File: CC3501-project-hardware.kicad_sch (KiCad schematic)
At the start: 0 parts

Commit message: Add USB C and make connections to ground.
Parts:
- added J1: USB_C_Receptacle_USB2.0_16P, Connector_USB:USB_C_Receptacle_G-Switch_GT-USB-7010ASV, symbol Connector:USB_C_Receptacle_USB2.0_16P
- added R1, R2: 5K1, Resistor_SMD:R_01005_0402Metric, symbol Device:R
- added U1: RP2040, Package_DFN_QFN:QFN-56-1EP_7x7mm_P0.4mm_EP3.2x3.2mm, symbol MCU_RaspberryPi:RP2040
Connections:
- new net: U1.1 (IOVDD), U1.10 (IOVDD), U1.22 (IOVDD), U1.33 (IOVDD), U1.42 (IOVDD), U1.49 (IOVDD)
- new net: U1.23 (DVDD), U1.50 (DVDD)
- new net: J1.A5 (CC1), R2.1
- new net: J1.B5 (CC2), R1.1
- new net: J1.A4 (VBUS), J1.A9 (VBUS), J1.B4 (VBUS), J1.B9 (VBUS)
- new net GND: J1.A1 (GND), J1.A12 (GND), J1.B1 (GND), J1.B12 (GND), J1.SH (SHIELD), R1.2, R2.2
- new net USB_D_N: J1.A7 (D-), J1.B7 (D-)
- new net USB_D_P: J1.A6 (D+), J1.B6 (D+)
- no-connect marks 0 -> 2

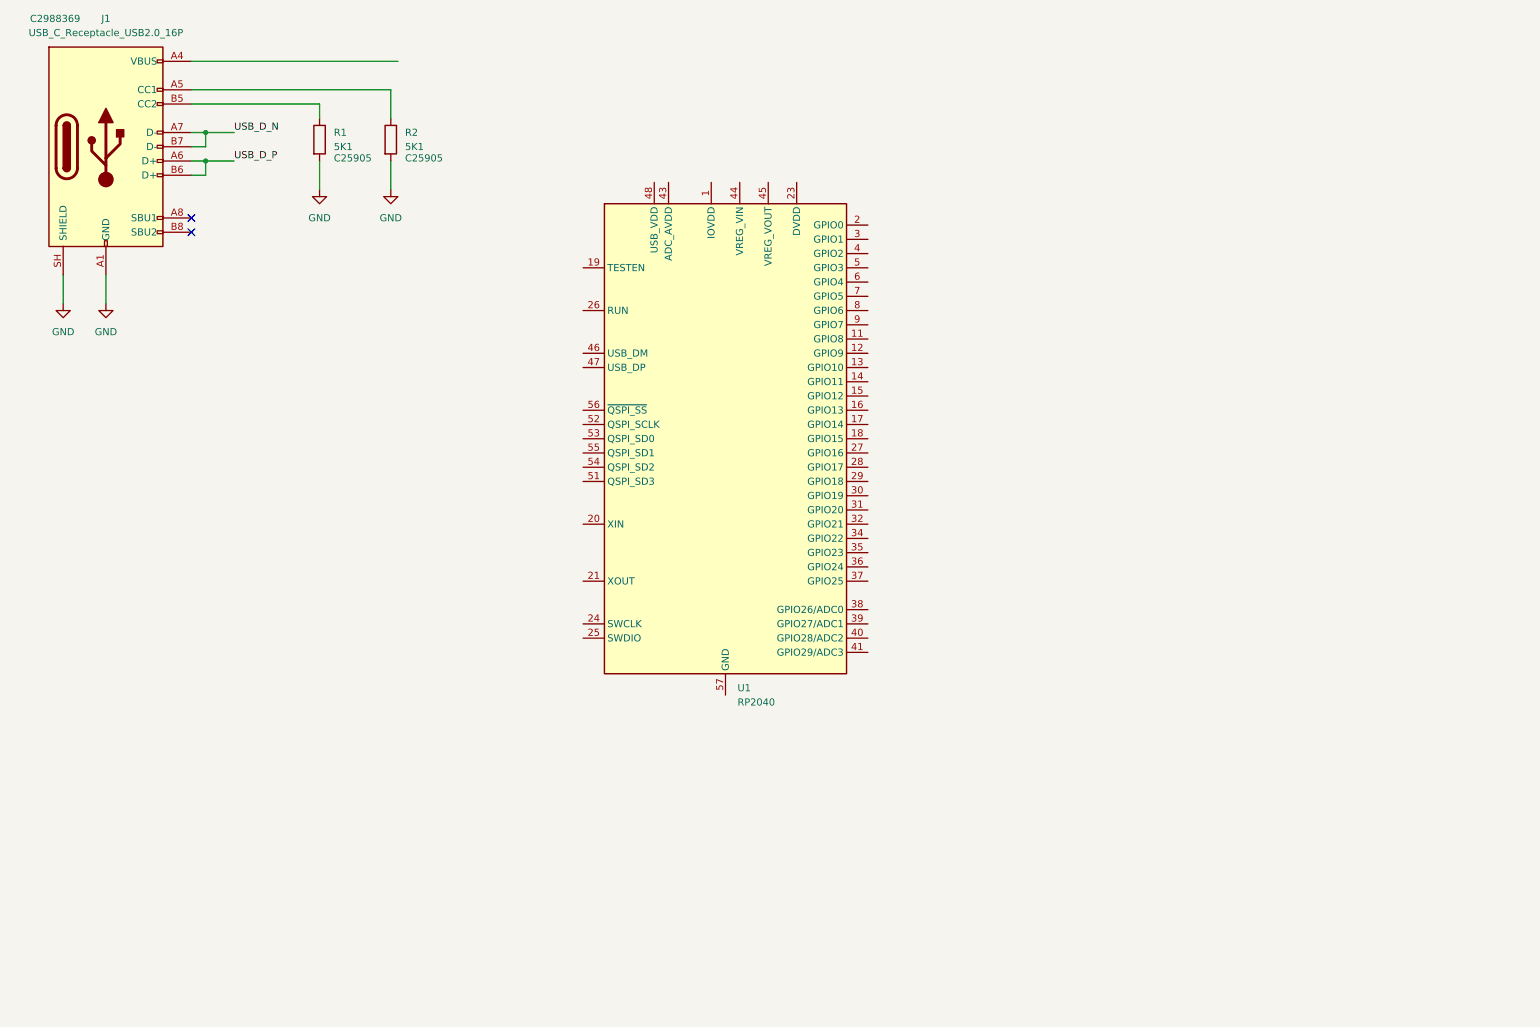
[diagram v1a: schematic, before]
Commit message: Add voltage regulator to USB input.
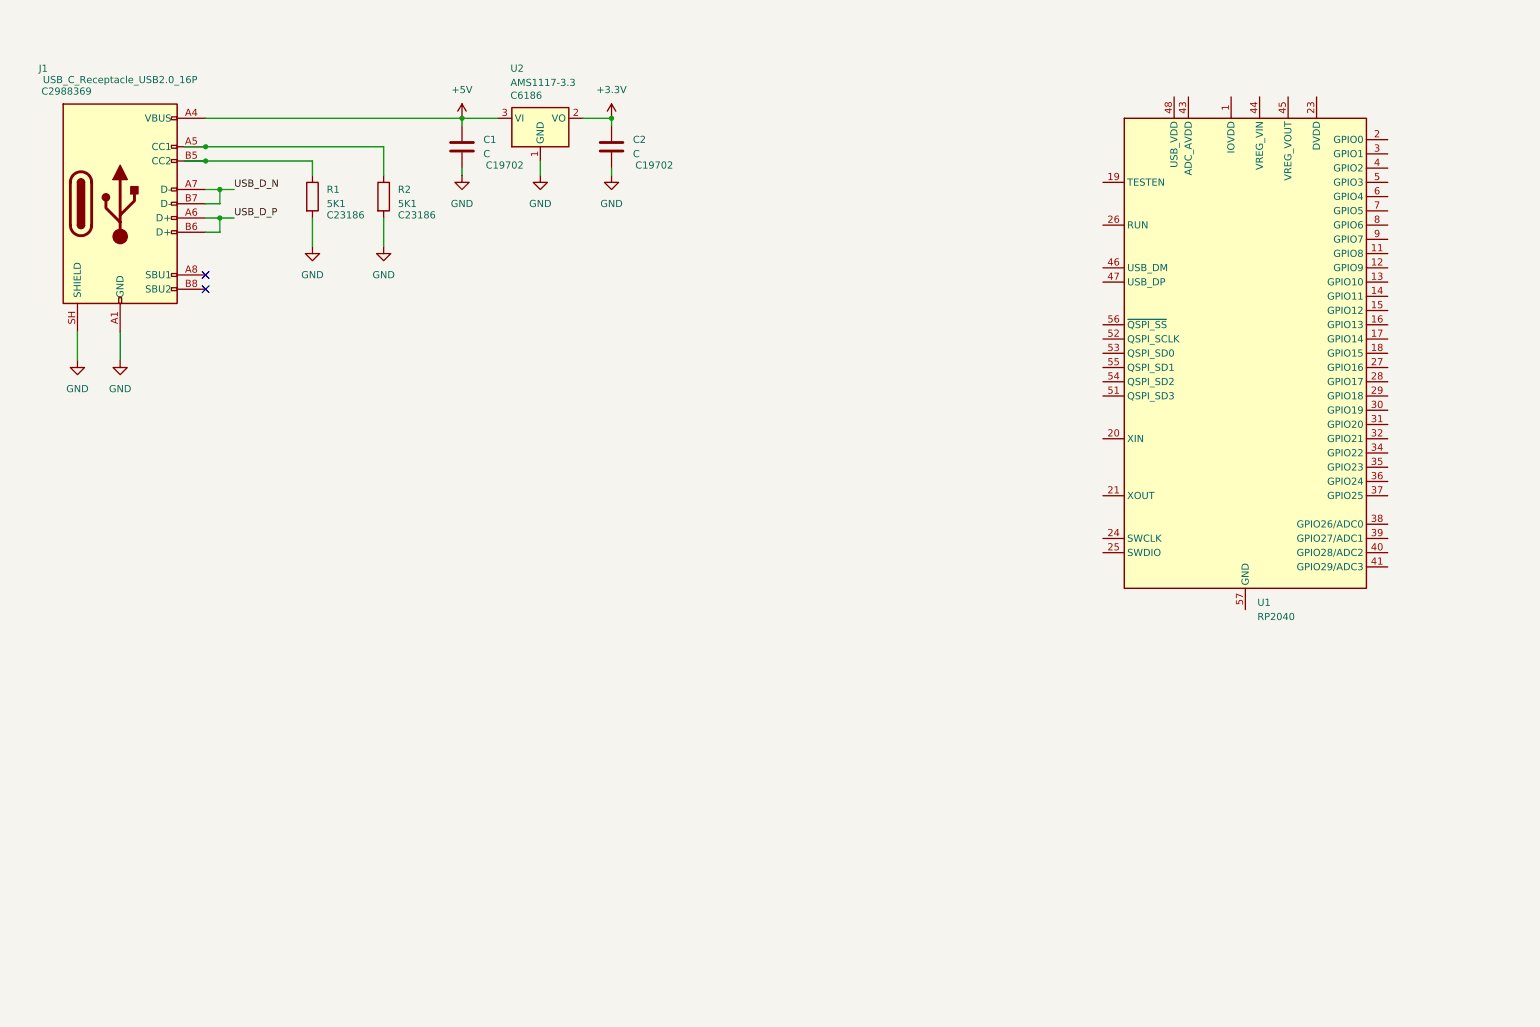
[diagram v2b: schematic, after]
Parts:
- added C1, C2: C, Capacitor_SMD:C_0201_0603Metric, symbol Device:C
- added U2: AMS1117-3.3, Package_TO_SOT_SMD:SOT-223-3_TabPin2, symbol Regulator_Linear:AMS1117-3.3
- R1, R2: footprint Resistor_SMD:R_01005_0402Metric -> Resistor_SMD:R_0201_0603Metric; LSCS PN C25905 -> C23186
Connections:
- net GND: now also C1.2, C2.2, U2.1 (GND)
- net +5V: now reaches J1.A4 (VBUS), J1.A9 (VBUS), J1.B4 (VBUS), J1.B9 (VBUS)
- net +5V: now also C1.1, U2.3 (VI)
- new net +3.3V: C2.1, U2.2 (VO)
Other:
- moved on the sheet: J1, R1, U1

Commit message: Add connection from USB DN/DP pins to RP2040 and include series 27R resisotor.
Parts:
- added R3, R4: 27R, Resistor_SMD:R_0201_0603Metric, symbol Device:R
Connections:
- net USB_D_N: now also R3.2
- net USB_D_P: now also R4.2
- net at U1.46 (USB_DM): now also R3.1
- net at U1.47 (USB_DP): now also R4.1

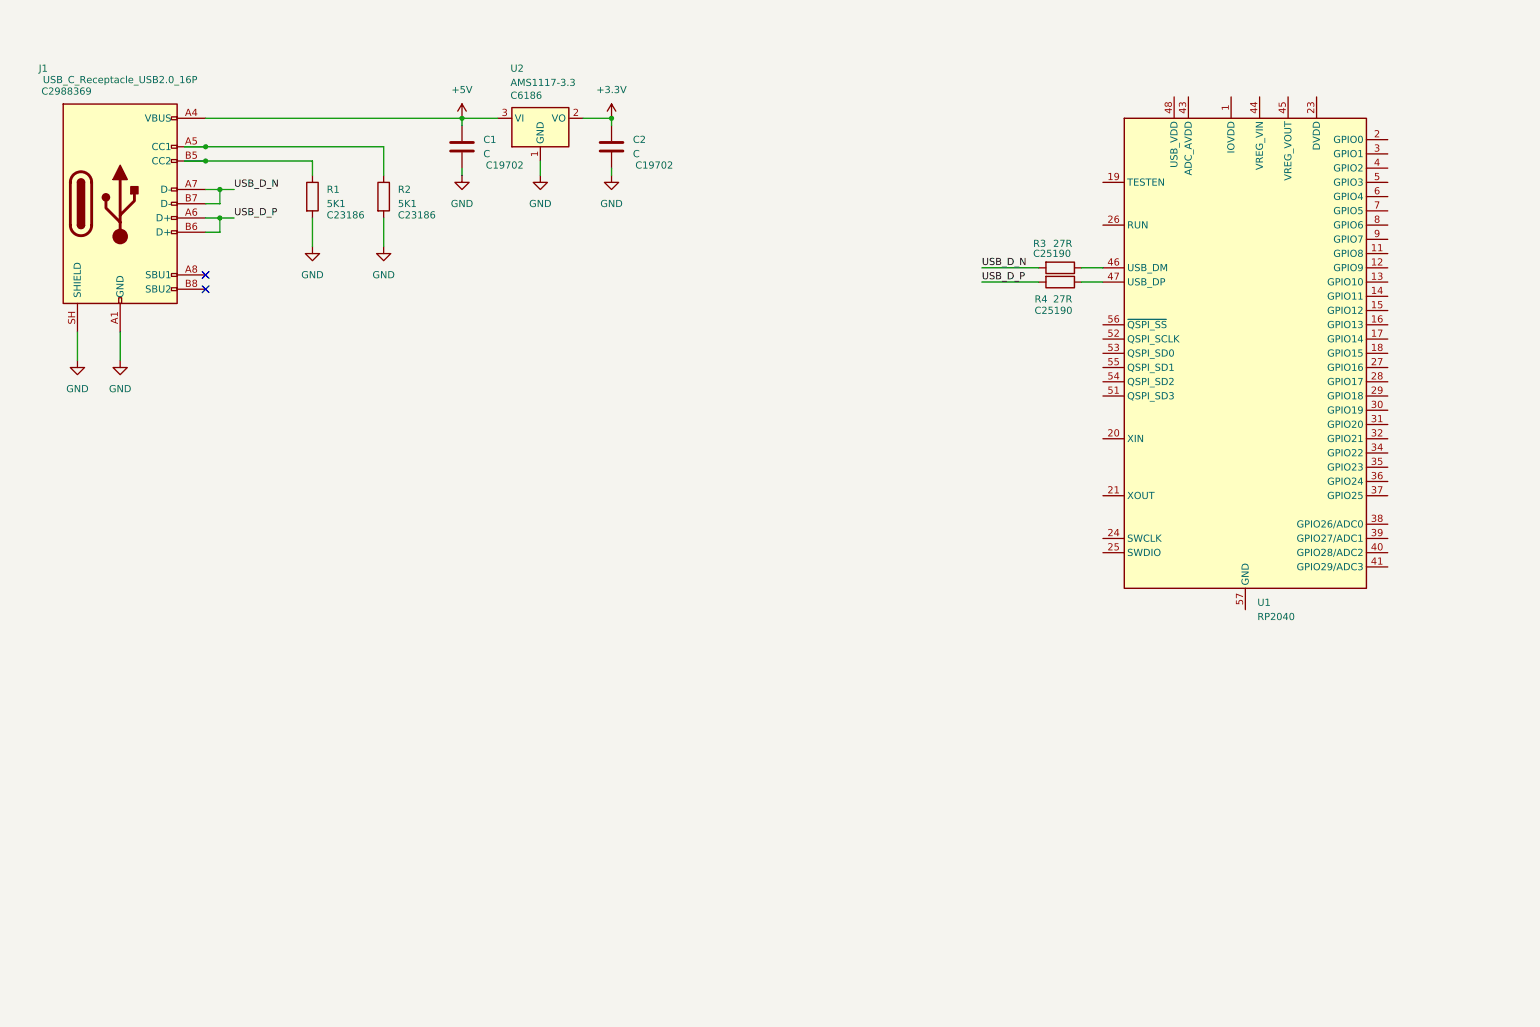
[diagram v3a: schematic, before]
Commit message: Added LCD, Load Cell Amplifier and Temp Sensors to schematic and made connections to RP2040.
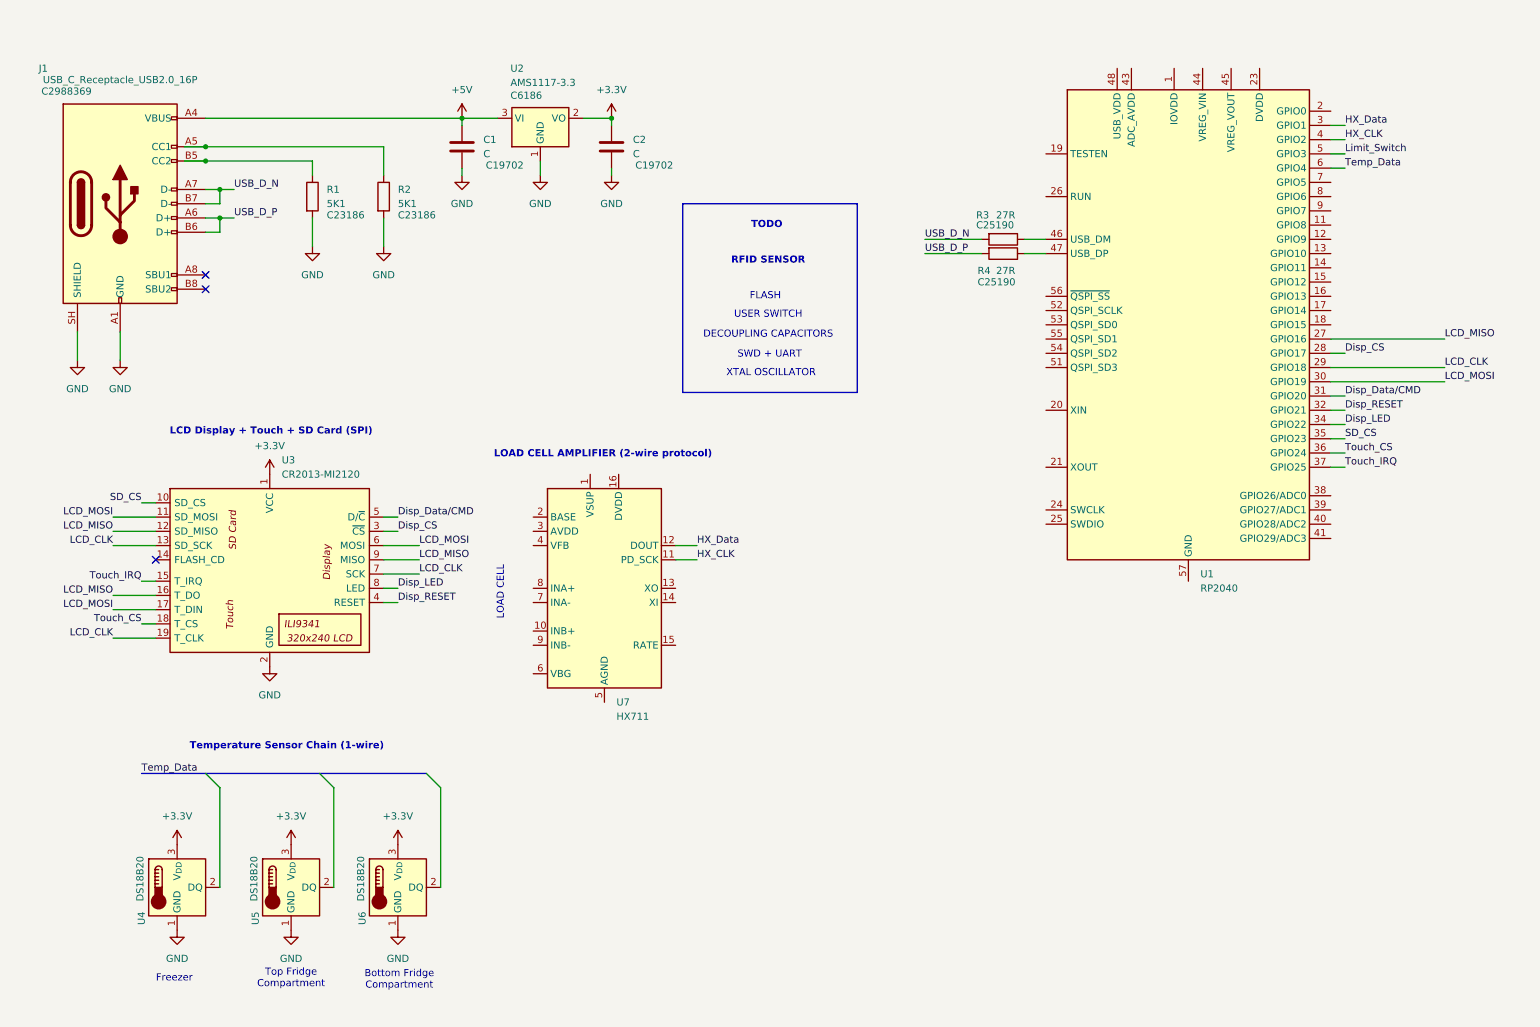
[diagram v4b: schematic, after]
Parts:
- added U3: CR2013-MI2120, Display:CR2013-MI2120, symbol Driver_Display:CR2013-MI2120
- added U4, U5, U6: DS18B20, Package_TO_SOT_THT:TO-92_Inline, symbol Sensor_Temperature:DS18B20
- added U7: HX711, Package_SO:SOIC-16_3.9x9.9mm_P1.27mm, symbol Analog_ADC:HX711
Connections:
- net +3.3V: now also U3.1 (VCC), U4.3 (V_{DD}), U5.3 (V_{DD}), U6.3 (V_{DD})
- net GND: now also U3.2 (GND), U4.1 (GND), U5.1 (GND), U6.1 (GND)
- net LCD_MISO: now reaches U1.27 (GPIO16)
- net LCD_MISO: now also U3.12 (SD_MISO), U3.16 (T_DO), U3.9 (MISO)
- net Disp_CS: now reaches U1.28 (GPIO17)
- net Disp_CS: now also U3.3 (~{CS})
- net LCD_CLK: now reaches U1.29 (GPIO18)
- net LCD_CLK: now also U3.13 (SD_SCK), U3.19 (T_CLK), U3.7 (SCK)
- net HX_Data: now reaches U1.3 (GPIO1)
- net HX_Data: now also U7.12 (DOUT)
- net LCD_MOSI: now reaches U1.30 (GPIO19)
- net LCD_MOSI: now also U3.11 (SD_MOSI), U3.17 (T_DIN), U3.6 (MOSI)
- net Disp_Data/CMD: now reaches U1.31 (GPIO20)
- net Disp_Data/CMD: now also U3.5 (D/~{C})
- net Disp_RESET: now reaches U1.32 (GPIO21)
- net Disp_RESET: now also U3.4 (RESET)
- net Disp_LED: now reaches U1.34 (GPIO22)
- net Disp_LED: now also U3.8 (LED)
- net SD_CS: now reaches U1.35 (GPIO23)
- net SD_CS: now also U3.10 (SD_CS)
- net Touch_CS: now reaches U1.36 (GPIO24)
- net Touch_CS: now also U3.18 (T_CS)
- net Touch_IRQ: now reaches U1.37 (GPIO25)
- net Touch_IRQ: now also U3.15 (T_IRQ)
- net HX_CLK: now reaches U1.4 (GPIO2)
- net HX_CLK: now also U7.11 (PD_SCK)
- net Limit_Switch: now reaches U1.5 (GPIO3)
- net Temp_Data: now reaches U1.6 (GPIO4)
- no-connect marks 2 -> 3
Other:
- note added: "Bottom Fridge Compartment"
- note added: "DECOUPLING CAPACITORS"
- note added: "FLASH"
- note added: "Freezer"
- note added: "LCD Display + Touch + SD Card (SPI)"
- note added: "LOAD CELL"
- note added: "LOAD CELL AMPLIFIER (2-wire protocol)"
- note added: "RFID SENSOR"
- note added: "SWD + UART"
- note added: "TODO"
- note added: "Temperature Sensor Chain (1-wire)"
- note added: "Top Fridge Compartment"
- note added: "USER SWITCH"
- note added: "XTAL OSCILLATOR"
- moved on the sheet: R3, R4, U1

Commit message: Add JLC part number to HX711
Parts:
- U7: LSCS PN (none) -> C6705483
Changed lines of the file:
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@@
+			)
+		)
+		(property "LSCS PN" "C6705483"
+			(at 116.84 115.57 0)
+			(hide yes)
+			(show_name no)
+			(do_not_autoplace no)
+			(effects
+				(font
+					(size 1.27 1.27)
+				)
 			)
 		)

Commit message: Add annotations for future considerations.
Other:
- note added: "Decouple Caps"
- note added: "LOAD CELL ADC (2-wire protocol)"
- note added: "NEED PULL UPS"
- note added: "Need to decide how to power temp sensors (3.3V power or through parasitic power, see datasheet)"
- note removed: "LOAD CELL AMPLIFIER (2-wire protocol)"
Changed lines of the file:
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@@
+		)
+	)
+	(text "Decouple Caps"
+		(exclude_from_sim no)
+		(at 59.944 153.67 0)
+		(effects
+			(font
+				(size 1.27 1.27)
+				(color 255 0 19 1)
+			)
 		)
 	)
@@
 		)
 	)
+	(text "NEED\nPULL UPS"
+		(exclude_from_sim no)
+		(at 18.288 111.252 0)
+		(effects
+			(font
+				(size 1.27 1.27)
+				(color 255 0 19 1)
+			)
+		)
+	)
 	(text "FLASH"
 		(exclude_from_sim no)
@@
 			(font
 				(size 1.27 1.27)
+			)
+		)
+	)
+	(text "Need to decide how to power temp sensors\n(3.3V power or through parasitic power, see datasheet)"
+		(exclude_from_sim no)
+		(at 56.642 145.288 0)
+		(effects
+			(font
+				(size 1.27 1.27)
+				(color 255 0 19 1)
 			)
 		)
@@
 		)
 	)
+	(text "Decouple Caps"
+		(exclude_from_sim no)
+		(at 50.038 92.202 0)
+		(effects
+			(font
+				(size 1.27 1.27)
+				(color 255 0 19 1)
+			)
+		)
+	)
 	(text "Bottom Fridge\nCompartment"
 		(exclude_from_sim no)
@@
 		)
 	)
-	(text "LOAD CELL AMPLIFIER (2-wire protocol)"
+	(text "LOAD CELL ADC (2-wire protocol)"
 		(exclude_from_sim no)
 		(at 116.586 91.694 0)
@@
 		)
 	)
+	(text "NEED\nPULL UPS"
+		(exclude_from_sim no)
+		(at 85.344 121.92 0)
+		(effects
+			(font
+				(size 1.27 1.27)
+				(color 255 0 19 1)
+			)
+		)
+	)
 	(text "SWD + UART"
 		(exclude_from_sim no)
@@
 	(text "Temperature Sensor Chain (1-wire)"
 		(exclude_from_sim no)
-		(at 60.198 143.764 0)
+		(at 59.182 141.478 0)
 		(effects
 			(font
@@
 		(property "LSCS PN" "C6705483"
 			(at 116.84 115.57 0)
-			(hide yes)
-			(show_name no)
-			(do_not_autoplace no)
+			(show_name no)
+			(do_not_autoplace no)
